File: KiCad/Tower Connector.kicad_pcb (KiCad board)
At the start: 2 copper layers, 110 x 50 mm, 6 parts, among them J1 Conn_01x03_Socket

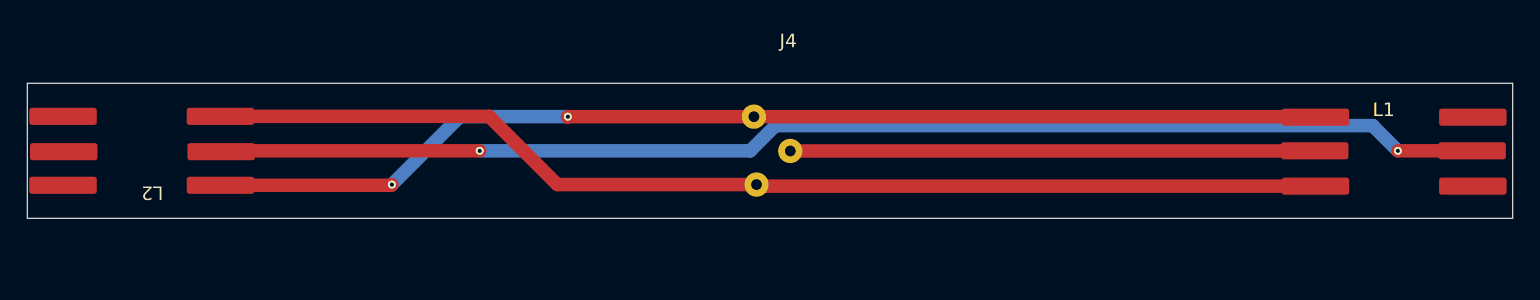
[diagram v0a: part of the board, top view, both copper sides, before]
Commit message: Refactored to separate PS arm from tower connector
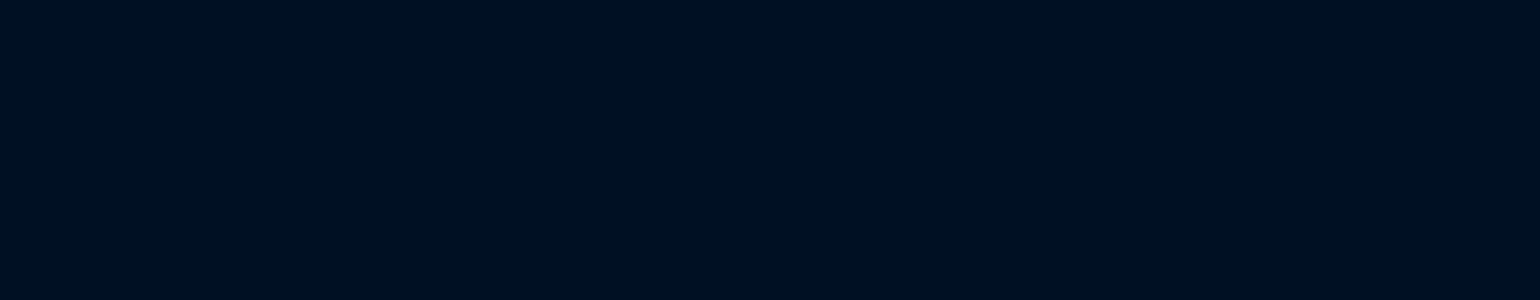
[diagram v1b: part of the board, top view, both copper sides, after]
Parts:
- removed J4: ~, My_Library:Staggered_3_pin_conn
- removed L1, L2: ~, My_Library:strip_WS2212
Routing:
- net Net-(L1-Dout): track 94.2 -> 0.00 mm, vias 2 -> 0
- net Net-(J4-Gnd): track 83.3 -> 0.00 mm, vias 2 -> 0
- net Net-(J4-Vcc): track 83.2 -> 0.00 mm
- net Net-(J4-Dout): track 38.8 -> 0.00 mm
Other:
- board size 110 x 50 mm -> 74 x 12 mm

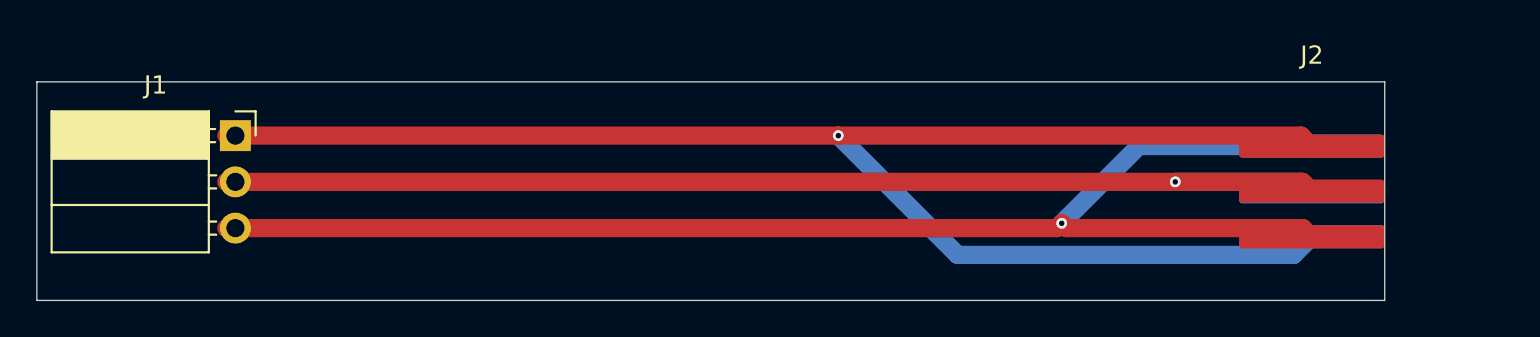
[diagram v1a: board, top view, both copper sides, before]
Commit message: Length adjusted to new cameras bracket
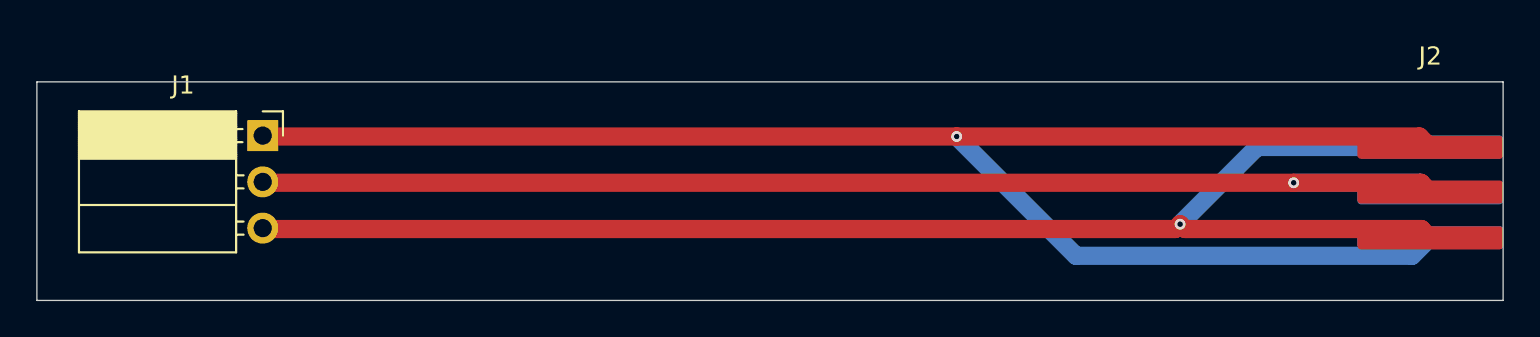
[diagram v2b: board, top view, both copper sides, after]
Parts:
- moved J2 6.50 mm to (176.5, 97.1)
- moved J3 6.50 mm to (176.5, 111.0)
- moved J1 1.50 mm to (112.4, 101.0)
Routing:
- net Net-(J1-Pin_3): track 75.8 -> 80.3 mm
- net Net-(J1-Pin_1): track 89.0 -> 93.5 mm
- net Net-(J1-Pin_2): track 67.9 -> 72.4 mm
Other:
- board size 74 x 12 mm -> 80.5 x 12 mm
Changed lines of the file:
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@@
 	(footprint "Connector_PinSocket_2.54mm:PinSocket_1x03_P2.54mm_Horizontal"
 		(layer "F.Cu")
-		(at 110.9 100.95)
+		(at 112.4 100.95)
 		(descr "Through hole angled socket strip, 1x03, 2.54mm pitch, 8.51mm socket length, single row (from Kicad 4.0.7), script generated")
 		(tags "Through hole angled socket strip THT 1x03 2.54mm single row")
@@
 	(footprint "My_footprints_Library:PCB_EDGE"
 		(layer "F.Cu")
-		(at 170 97.0404)
+		(at 176.5 97.0904)
 		(property "Reference" "J2"
 			(at 0 -0.5 0)
@@
 	(footprint "My_footprints_Library:PCB_EDGE"
 		(layer "B.Cu")
-		(at 170 111)
+		(at 176.5 111.05)
 		(property "Reference" "J3"
 			(at 0 0.5 180)
@@
 	(gr_rect
 		(start 100 98)
-		(end 174 110)
+		(end 180.5 110)
 		(stroke
 			(width 0.05)
@@
 	)
 	(segment
-		(start 110.4 100.95)
-		(end 144 100.95)
+		(start 150.5 101)
+		(end 175.9096 101)
 		(width 1)
 		(layer "F.Cu")
@@
 	)
 	(segment
-		(start 144 100.95)
-		(end 169.4096 100.95)
+		(start 175.9096 101)
+		(end 176.5 101.5904)
 		(width 1)
 		(layer "F.Cu")
@@
 	)
 	(segment
-		(start 169.4096 100.95)
-		(end 170 101.5404)
+		(start 112.45 101)
+		(end 150.5 101)
 		(width 1)
 		(layer "F.Cu")
 		(net "Net-(J1-Pin_1)")
 	)
+	(segment
+		(start 112.4 100.95)
+		(end 112.45 101)
+		(width 1)
+		(layer "F.Cu")
+		(net "Net-(J1-Pin_1)")
+	)
 	(via
-		(at 144 100.95)
+		(at 150.5 101)
 		(size 0.6)
 		(drill 0.3)
@@
 	)
 	(segment
-		(start 144 100.95)
-		(end 150.55 107.5)
+		(start 150.5 101)
+		(end 157.05 107.55)
 		(width 1)
 		(layer "B.Cu")
@@
 	)
 	(segment
-		(start 169 107.5)
-		(end 170 106.5)
+		(start 175.5 107.55)
+		(end 176.5 106.55)
 		(width 1)
 		(layer "B.Cu")
@@
 	)
 	(segment
-		(start 150.55 107.5)
-		(end 169 107.5)
+		(start 157.05 107.55)
+		(end 175.5 107.55)
 		(width 1)
 		(layer "B.Cu")
@@
 	)
 	(segment
-		(start 110.4 103.49)
-		(end 162.5 103.49)
+		(start 175.99 103.54)
+		(end 176.5 104.05)
 		(width 1)
 		(layer "F.Cu")
@@
 	)
 	(segment
-		(start 169.49 103.49)
-		(end 170 104)
+		(start 169 103.54)
+		(end 175.99 103.54)
 		(width 1)
 		(layer "F.Cu")
@@
 	)
 	(segment
-		(start 162.5 103.49)
-		(end 169.49 103.49)
-		(width 1)
+		(start 176.2604 103.8104)
+		(end 176.5 104.05)
+		(width 0.2)
 		(layer "F.Cu")
 		(net "Net-(J1-Pin_2)")
 	)
 	(segment
-		(start 169.7604 103.7604)
-		(end 170 104)
-		(width 0.2)
+		(start 112.45 103.54)
+		(end 169 103.54)
+		(width 1)
 		(layer "F.Cu")
 		(net "Net-(J1-Pin_2)")
 	)
+	(segment
+		(start 112.4 103.49)
+		(end 112.45 103.54)
+		(width 1)
+		(layer "F.Cu")
+		(net "Net-(J1-Pin_2)")
+	)
 	(via
-		(at 162.5 103.49)
+		(at 169 103.54)
 		(size 0.6)
 		(drill 0.3)
@@
 	)
 	(segment
-		(start 169.4496 103.49)
-		(end 170 104.0404)
+		(start 175.9496 103.54)
+		(end 176.5 104.0904)
 		(width 1)
 		(layer "B.Cu")
@@
 	)
 	(segment
-		(start 162.5 103.49)
-		(end 169.4496 103.49)
+		(start 169 103.54)
+		(end 175.9496 103.54)
 		(width 1)
 		(layer "B.Cu")
@@
 	)
 	(segment
-		(start 169.5154 106.03)
-		(end 170 106.5146)
+		(start 176.0154 106.08)
+		(end 176.5 106.5646)
 		(width 1)
 		(layer "F.Cu")
@@
 	)
 	(segment
-		(start 110.4 106.03)
-		(end 156 106.03)
+		(start 163.03 106.08)
+		(end 176.0154 106.08)
 		(width 1)
 		(layer "F.Cu")
@@
 	)
 	(segment
-		(start 156.53 106.03)
-		(end 169.5154 106.03)
+		(start 162.5 106.08)
+		(end 162.765 105.815)
 		(width 1)
 		(layer "F.Cu")
@@
 	)
 	(segment
-		(start 156.265 105.765)
-		(end 156.53 106.03)
+		(start 162.765 105.815)
+		(end 163.03 106.08)
 		(width 1)
 		(layer "F.Cu")
@@
 	)
 	(segment
-		(start 169.7858 106.3004)
-		(end 170 106.5146)
+		(start 112.4 106.03)
+		(end 112.45 106.08)
+		(width 1)
+		(layer "F.Cu")
+		(net "Net-(J1-Pin_3)")
+	)
+	(segment
+		(start 176.2858 106.3504)
+		(end 176.5 106.5646)
 		(width 0.2)
 		(layer "F.Cu")
@@
 	)
 	(segment
-		(start 156 106.03)
-		(end 156.265 105.765)
+		(start 112.45 106.08)
+		(end 162.5 106.08)
 		(width 1)
 		(layer "F.Cu")
@@
 	)
 	(via
-		(at 156.265 105.765)
+		(at 162.765 105.815)
 		(size 0.6)
 		(drill 0.3)
@@
 	)
 	(segment
-		(start 156.265 105.765)
-		(end 160.5042 101.5258)
+		(start 162.765 105.815)
+		(end 167.0042 101.5758)
 		(width 1)
 		(layer "B.Cu")
@@
 	)
 	(segment
-		(start 160.5042 101.5258)
-		(end 170 101.5258)
+		(start 167.0042 101.5758)
+		(end 176.5 101.5758)
 		(width 1)
 		(layer "B.Cu")
